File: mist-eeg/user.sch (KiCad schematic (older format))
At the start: 18 parts, among them SW1 START, SW2 USER

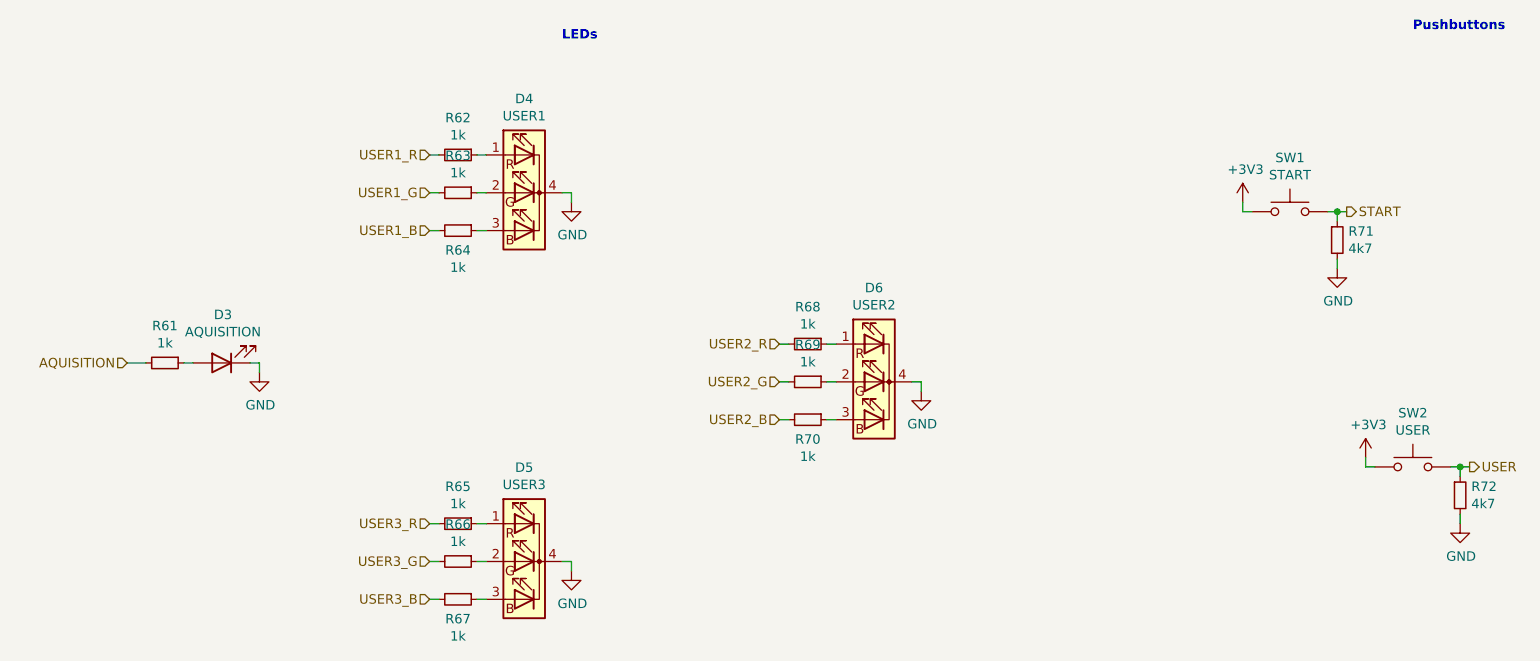
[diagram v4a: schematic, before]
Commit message: Switch to POL switching regulator to accelerate production of the board
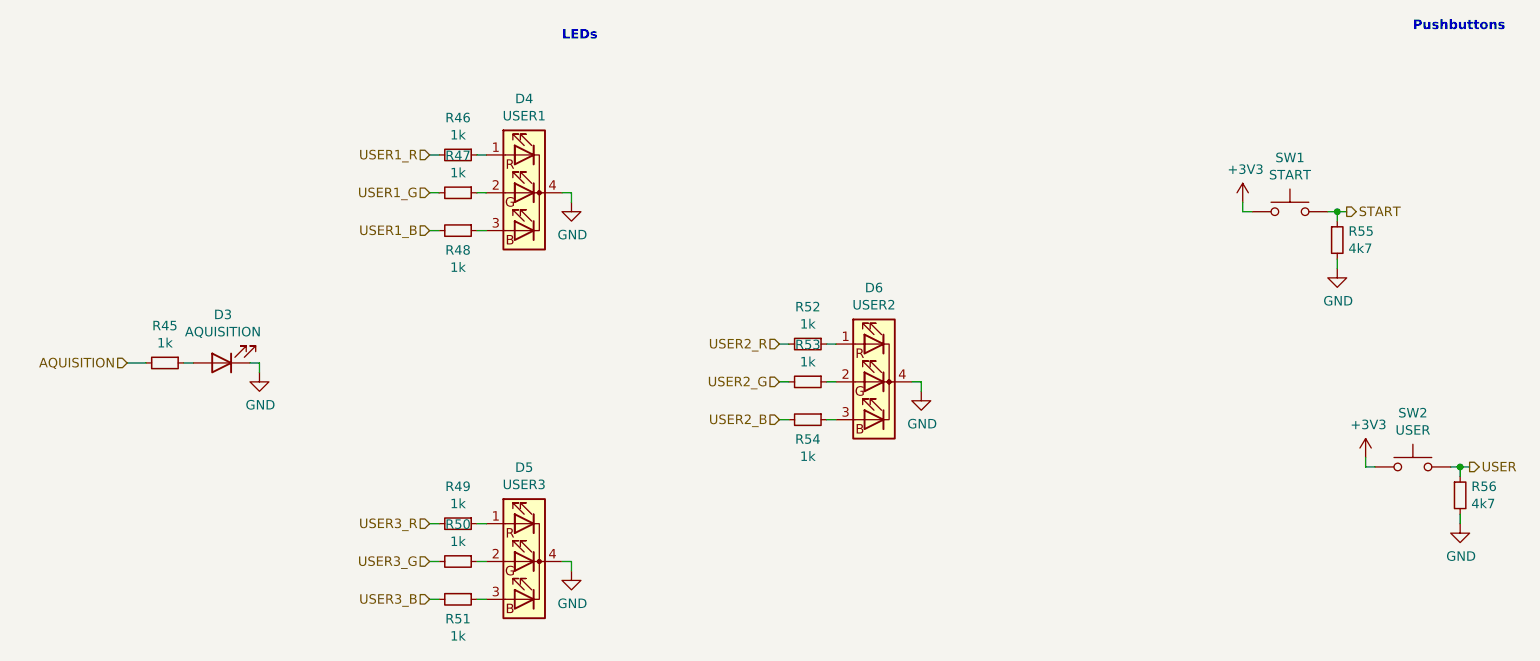
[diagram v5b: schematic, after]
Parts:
- renumbered R61 to R45, R62 to R46, R63 to R47, R64 to R48, R65 to R49, R66 to R50, R67 to R51, R68 to R52, R69 to R53, R70 to R54, R71 to R55, R72 to R56
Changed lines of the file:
@@
 $Descr USLetter 11000 8500
 encoding utf-8
-Sheet 9 11
+Sheet 6 8
 Title "Portiloop"
-Date "2021-08-03"
-Rev "1D"
+Date "2021-08-05"
+Rev "1E"
 Comp "MIST Lab"
 Comment1 "Designed by Xavier L'Heureux"
@@
 $EndComp
 $Comp
-L power:GND #PWR088
+L power:GND #PWR066
 U 1 1 60D255D9
 P 3750 3300
-F 0 "#PWR088" H 3750 3050 50  0001 C CNN
+F 0 "#PWR066" H 3750 3050 50  0001 C CNN
 F 1 "GND" H 3755 3127 50  0000 C CNN
 F 2 "" H 3750 3300 50  0001 C CNN
@@
 	3750 3250 3700 3250
 $Comp
-L Device:R_Small R62
+L Device:R_Small R46
 U 1 1 60D26A9C
 P 3150 3050
-F 0 "R62" V 2954 3050 50  0000 C CNN
+F 0 "R46" V 2954 3050 50  0000 C CNN
 F 1 "1k" V 3045 3050 50  0000 C CNN
 F 2 "Resistor_SMD:R_0402_1005Metric" H 3150 3050 50  0001 C CNN
@@
 	3000 3050 3050 3050
 $Comp
-L Device:R_Small R63
+L Device:R_Small R47
 U 1 1 60D27725
 P 3150 3250
-F 0 "R63" V 2954 3250 50  0000 C CNN
+F 0 "R47" V 2954 3250 50  0000 C CNN
 F 1 "1k" V 3045 3250 50  0000 C CNN
 F 2 "Resistor_SMD:R_0402_1005Metric" H 3150 3250 50  0001 C CNN
@@
 	3000 3250 3050 3250
 $Comp
-L Device:R_Small R64
+L Device:R_Small R48
 U 1 1 60D27A38
 P 3150 3450
-F 0 "R64" V 3254 3450 50  0000 C CNN
+F 0 "R48" V 3254 3450 50  0000 C CNN
 F 1 "1k" V 3345 3450 50  0000 C CNN
 F 2 "Resistor_SMD:R_0402_1005Metric" H 3150 3450 50  0001 C CNN
@@
 $EndComp
 $Comp
-L power:GND #PWR090
+L power:GND #PWR068
 U 1 1 60D29FC6
 P 5600 4300
-F 0 "#PWR090" H 5600 4050 50  0001 C CNN
+F 0 "#PWR068" H 5600 4050 50  0001 C CNN
 F 1 "GND" H 5605 4127 50  0000 C CNN
 F 2 "" H 5600 4300 50  0001 C CNN
@@
 	5600 4250 5550 4250
 $Comp
-L Device:R_Small R68
+L Device:R_Small R52
 U 1 1 60D29FCE
 P 5000 4050
-F 0 "R68" V 4804 4050 50  0000 C CNN
+F 0 "R52" V 4804 4050 50  0000 C CNN
 F 1 "1k" V 4895 4050 50  0000 C CNN
 F 2 "Resistor_SMD:R_0402_1005Metric" H 5000 4050 50  0001 C CNN
@@
 	4850 4050 4900 4050
 $Comp
-L Device:R_Small R69
+L Device:R_Small R53
 U 1 1 60D29FD7
 P 5000 4250
-F 0 "R69" V 4804 4250 50  0000 C CNN
+F 0 "R53" V 4804 4250 50  0000 C CNN
 F 1 "1k" V 4895 4250 50  0000 C CNN
 F 2 "Resistor_SMD:R_0402_1005Metric" H 5000 4250 50  0001 C CNN
@@
 	4850 4250 4900 4250
 $Comp
-L Device:R_Small R70
+L Device:R_Small R54
 U 1 1 60D29FE0
 P 5000 4450
-F 0 "R70" V 5104 4450 50  0000 C CNN
+F 0 "R54" V 5104 4450 50  0000 C CNN
 F 1 "1k" V 5195 4450 50  0000 C CNN
 F 2 "Resistor_SMD:R_0402_1005Metric" H 5000 4450 50  0001 C CNN
@@
 $EndComp
 $Comp
-L power:GND #PWR089
+L power:GND #PWR067
 U 1 1 60D2CF81
 P 3750 5250
-F 0 "#PWR089" H 3750 5000 50  0001 C CNN
+F 0 "#PWR067" H 3750 5000 50  0001 C CNN
 F 1 "GND" H 3755 5077 50  0000 C CNN
 F 2 "" H 3750 5250 50  0001 C CNN
@@
 	3750 5200 3700 5200
 $Comp
-L Device:R_Small R65
+L Device:R_Small R49
 U 1 1 60D2CF89
 P 3150 5000
-F 0 "R65" V 2954 5000 50  0000 C CNN
+F 0 "R49" V 2954 5000 50  0000 C CNN
 F 1 "1k" V 3045 5000 50  0000 C CNN
 F 2 "Resistor_SMD:R_0402_1005Metric" H 3150 5000 50  0001 C CNN
@@
 	3000 5000 3050 5000
 $Comp
-L Device:R_Small R66
+L Device:R_Small R50
 U 1 1 60D2CF92
 P 3150 5200
-F 0 "R66" V 2954 5200 50  0000 C CNN
+F 0 "R50" V 2954 5200 50  0000 C CNN
 F 1 "1k" V 3045 5200 50  0000 C CNN
 F 2 "Resistor_SMD:R_0402_1005Metric" H 3150 5200 50  0001 C CNN
@@
 	3000 5200 3050 5200
 $Comp
-L Device:R_Small R67
+L Device:R_Small R51
 U 1 1 60D2CF9B
 P 3150 5400
-F 0 "R67" V 3254 5400 50  0000 C CNN
+F 0 "R51" V 3254 5400 50  0000 C CNN
 F 1 "1k" V 3345 5400 50  0000 C CNN
 F 2 "Resistor_SMD:R_0402_1005Metric" H 3150 5400 50  0001 C CNN
@@
 	7800 3650 7800 3600
 $Comp
-L power:GND #PWR092
+L power:GND #PWR070
 U 1 1 60D6D004
 P 7800 3650
-F 0 "#PWR092" H 7800 3400 50  0001 C CNN
+F 0 "#PWR070" H 7800 3400 50  0001 C CNN
 F 1 "GND" H 7805 3477 50  0000 C CNN
 F 2 "" H 7800 3650 50  0001 C CNN
@@
 $EndComp
 $Comp
-L Device:R_Small R71
+L Device:R_Small R55
 U 1 1 60D6CBEB
 P 7800 3500
-F 0 "R71" H 7859 3546 50  0000 L CNN
+F 0 "R55" H 7859 3546 50  0000 L CNN
 F 1 "4k7" H 7859 3455 50  0000 L CNN
 F 2 "Resistor_SMD:R_0201_0603Metric" H 7800 3500 50  0001 C CNN
@@
 	2100 4200 2100 4150
 $Comp
-L power:GND #PWR087
+L power:GND #PWR065
 U 1 1 60D1F73E
 P 2100 4200
-F 0 "#PWR087" H 2100 3950 50  0001 C CNN
+F 0 "#PWR065" H 2100 3950 50  0001 C CNN
 F 1 "GND" H 2105 4027 50  0000 C CNN
 F 2 "" H 2100 4200 50  0001 C CNN
@@
 	1700 4150 1750 4150
 $Comp
-L Device:R_Small R61
+L Device:R_Small R45
 U 1 1 60D1C4D3
 P 1600 4150
-F 0 "R61" V 1404 4150 50  0000 C CNN
+F 0 "R45" V 1404 4150 50  0000 C CNN
 F 1 "1k" V 1495 4150 50  0000 C CNN
 F 2 "Resistor_SMD:R_0402_1005Metric" H 1600 4150 50  0001 C CNN
@@
 $EndComp
 $Comp
-L power:+3V3 #PWR091
+L power:+3V3 #PWR069
 U 1 1 61146B19
 P 7300 3300
-F 0 "#PWR091" H 7300 3150 50  0001 C CNN
+F 0 "#PWR069" H 7300 3150 50  0001 C CNN
 F 1 "+3V3" H 7315 3473 50  0000 C CNN
 F 2 "" H 7300 3300 50  0001 C CNN
@@
 	8450 5000 8450 4950
 $Comp
-L power:GND #PWR094
+L power:GND #PWR072
 U 1 1 61304D1F
 P 8450 5000
-F 0 "#PWR094" H 8450 4750 50  0001 C CNN
+F 0 "#PWR072" H 8450 4750 50  0001 C CNN
 F 1 "GND" H 8455 4827 50  0000 C CNN
 F 2 "" H 8450 5000 50  0001 C CNN
@@
 $EndComp
 $Comp
-L Device:R_Small R72
+L Device:R_Small R56
 U 1 1 61304D25
 P 8450 4850
-F 0 "R72" H 8509 4896 50  0000 L CNN
+F 0 "R56" H 8509 4896 50  0000 L CNN
 F 1 "4k7" H 8509 4805 50  0000 L CNN
 F 2 "Resistor_SMD:R_0201_0603Metric" H 8450 4850 50  0001 C CNN
@@
 $EndComp
 $Comp
-L power:+3V3 #PWR093
+L power:+3V3 #PWR071
 U 1 1 61304D31
 P 7950 4650
-F 0 "#PWR093" H 7950 4500 50  0001 C CNN
+F 0 "#PWR071" H 7950 4500 50  0001 C CNN
 F 1 "+3V3" H 7965 4823 50  0000 C CNN
 F 2 "" H 7950 4650 50  0001 C CNN
